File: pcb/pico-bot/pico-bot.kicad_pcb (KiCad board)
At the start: 2 copper layers, 58 parts, among them J1 Conn_01x02_Male, J2 Conn_01x06_Male, J3 Conn_01x06_Male, J4 Conn_01x06_Male, J5 Conn_01x06_Male, Q1 DMG2305UX, Q2 AOD417, SW1 SW_SPDT, SW2 SW_Push, SW3 SW_Push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

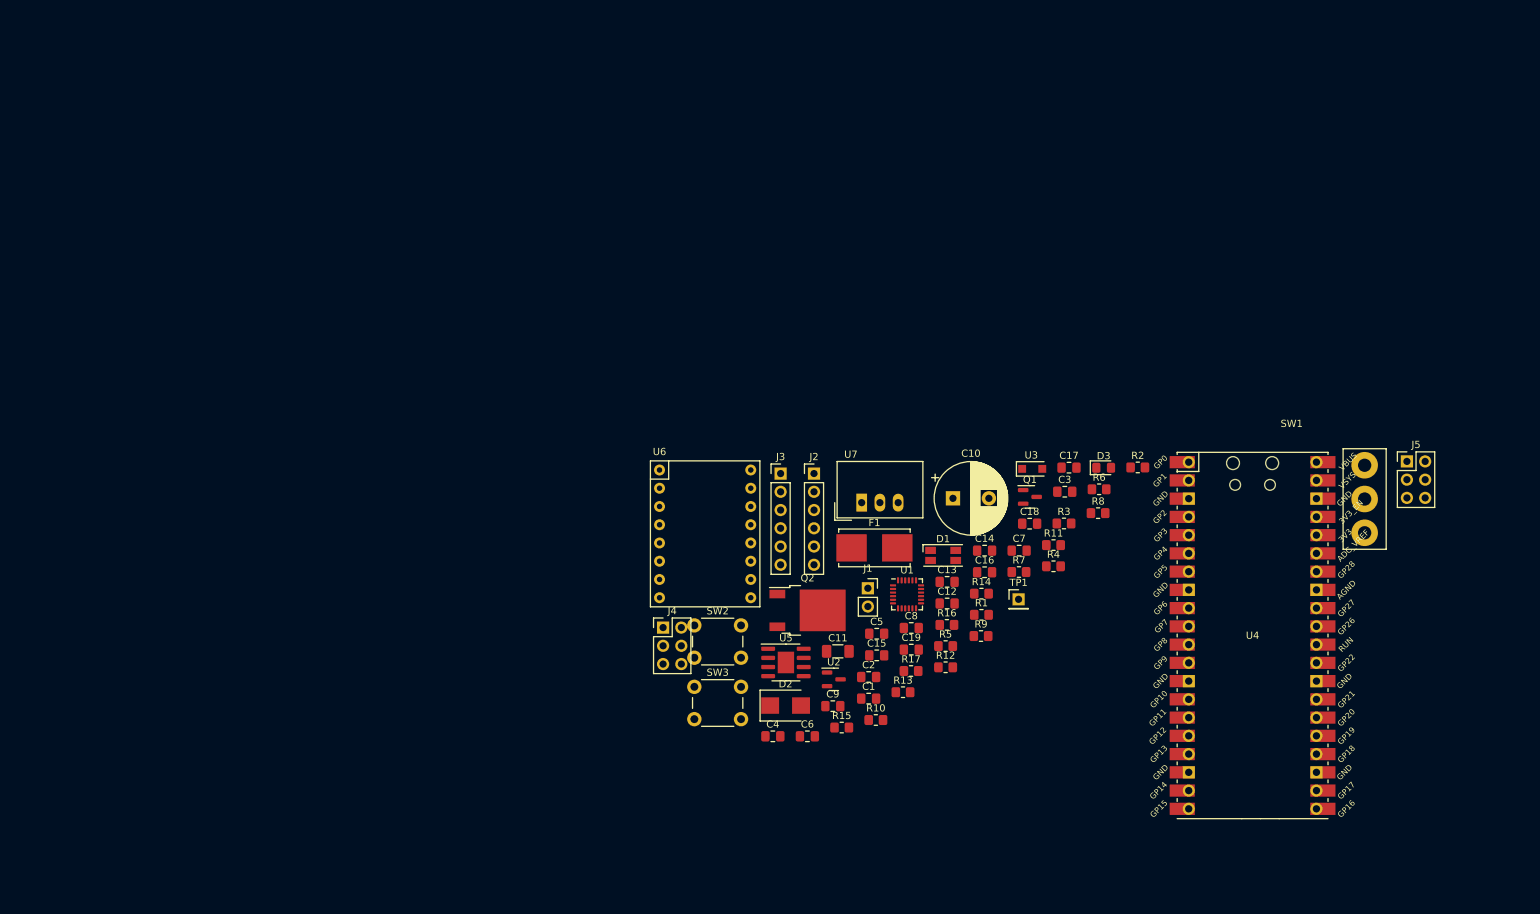
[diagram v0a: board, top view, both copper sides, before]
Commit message: Define mounting hole locations
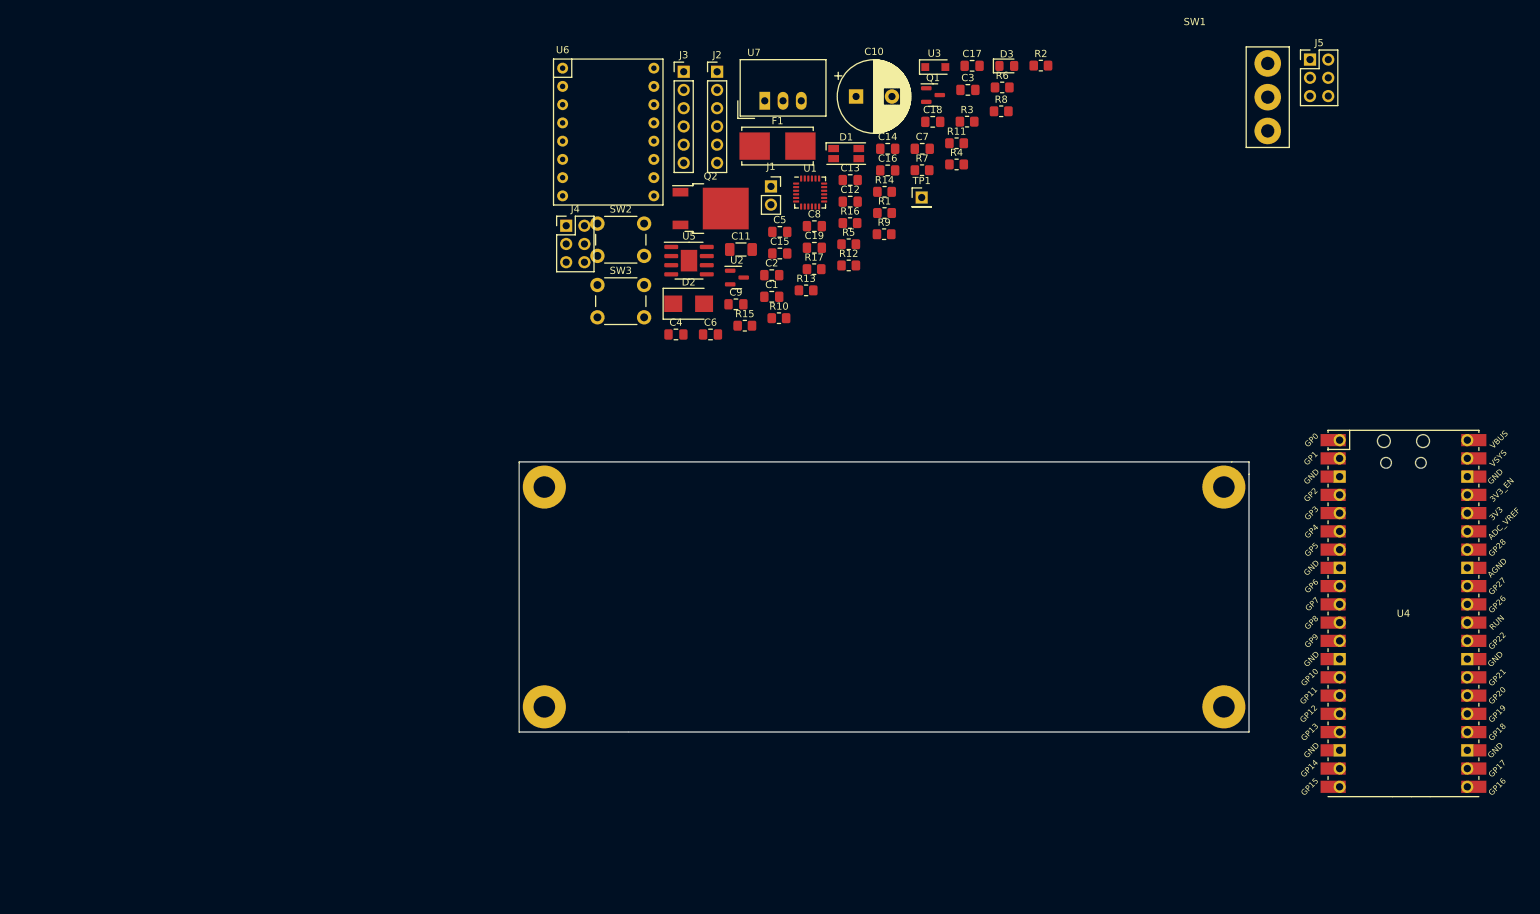
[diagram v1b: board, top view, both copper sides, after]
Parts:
- added REF**: MountingHole_3mm_Pad, MountingHole:MountingHole_3mm_Pad, F.Cu at (100.9, 109.1)
- added REF**: MountingHole_3mm_Pad, MountingHole:MountingHole_3mm_Pad, F.Cu at (100.9, 78.5)
- added REF**: MountingHole_3mm_Pad, MountingHole:MountingHole_3mm_Pad, F.Cu at (195.5, 78.5)
- added REF**: MountingHole_3mm_Pad, MountingHole:MountingHole_3mm_Pad, F.Cu at (195.5, 109.1)
- moved J5 57.5 mm to (207.5, 19.0)
- moved C1 57.5 mm to (132.6, 52.0)
- moved C11 57.5 mm to (128.3, 45.4)
- moved C13 57.5 mm to (143.5, 35.8)
- moved C15 57.5 mm to (133.7, 46.0)
- moved C3 57.5 mm to (159.9, 23.2)
- moved C4 57.5 mm to (119.2, 57.3)
- moved C5 57.5 mm to (133.7, 43.0)
- moved C6 57.5 mm to (124.0, 57.3)
- moved C8 57.5 mm to (138.5, 42.2)
- moved D2 57.5 mm to (121.0, 53.0)
- moved J1 57.5 mm to (132.4, 36.6)
- moved J2 57.5 mm to (125.0, 20.7)
- moved J3 57.5 mm to (120.3, 20.7)
- moved J4 57.5 mm to (103.9, 42.1)
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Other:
- board outline added: 101.6 x 37.6 mm

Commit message: Group circuits together on PCB
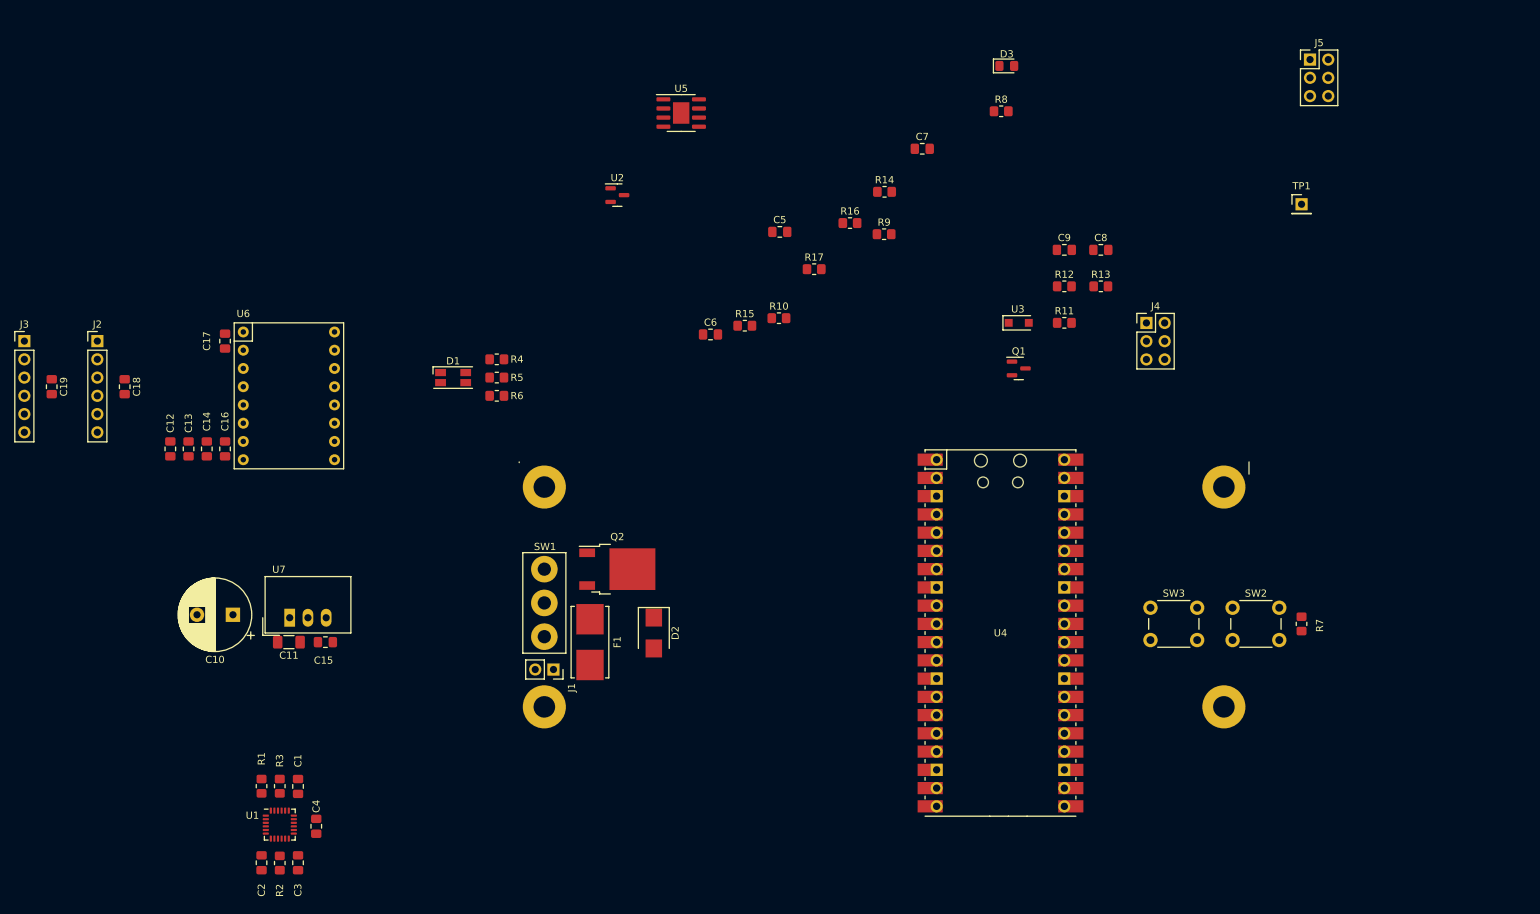
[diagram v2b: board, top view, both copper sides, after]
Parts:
- moved R2 153.5 mm to (64.1, 130.8), turned to 90 degrees
- moved C3 142.4 mm to (66.6, 130.8), turned to 90 degrees
- moved R3 133.1 mm to (64.1, 120.1), turned to 90 degrees
- moved SW1 122.9 mm to (100.9, 89.9)
- moved C18 118.4 mm to (42.5, 64.5), turned to -90 degrees
- moved R1 117.8 mm to (61.5, 120.1), turned to 90 degrees
- moved U1 114.9 mm to (64.1, 125.5)
- moved C10 112.8 mm to (57.5, 96.3), turned to 180 degrees
- moved C17 110.8 mm to (56.5, 58.2), turned to -90 degrees
- moved C2 108.3 mm to (61.5, 130.8), turned to 90 degrees
- moved C19 107.9 mm to (32.3, 64.5), turned to -90 degrees
- moved C14 103.6 mm to (53.9, 73.2), turned to 90 degrees
- moved SW2 103.3 mm to (196.7, 95.3)
- moved C12 100.7 mm to (48.8, 73.2), turned to 90 degrees
- moved C16 100.1 mm to (56.5, 73.2), turned to 90 degrees
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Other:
- board size 101.6 x 37.6 mm -> 101.6 x 1.7 mm

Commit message: Group undervoltage protection circuit components
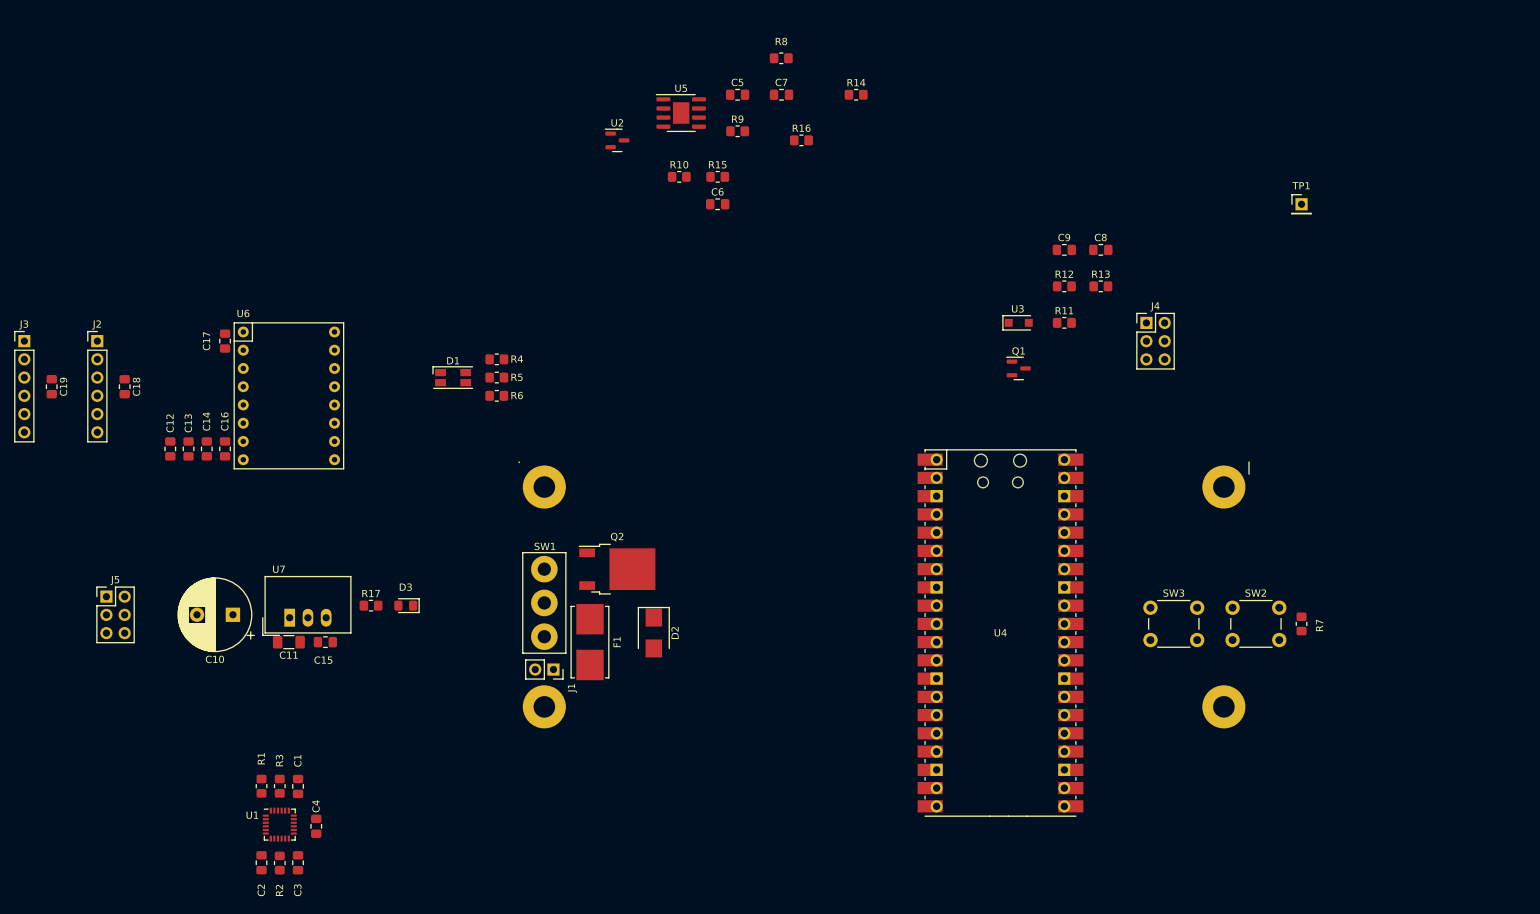
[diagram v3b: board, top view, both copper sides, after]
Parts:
- moved J5 183.5 mm to (39.9, 93.8)
- moved D3 112.5 mm to (81.6, 95.0), turned to 180 degrees
- moved R17 77.5 mm to (76.8, 95.0)
- moved R8 31.5 mm to (133.9, 18.8)
- moved R9 24.9 mm to (127.8, 29.0)
- moved R10 24.1 mm to (119.7, 35.3)
- moved R15 21.1 mm to (125.0, 35.3)
- moved C7 21.0 mm to (133.9, 23.9)
- moved C5 20.0 mm to (127.8, 23.9)
- moved C6 18.2 mm to (125.0, 39.1)
- moved R14 14.1 mm to (144.3, 23.9)
- moved R16 13.3 mm to (136.7, 30.2)
- moved U2 7.62 mm to (111.1, 30.2)
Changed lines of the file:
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@@
   )
   (footprint "Resistor_SMD:R_0805_2012Metric_Pad1.20x1.40mm_HandSolder" (layer "F.Cu")
-    (at 133.56 54.99)
+    (at 119.68 35.32)
     (descr "Resistor SMD 0805 (2012 Metric), square (rectangular) end terminal, IPC_7351 nominal with elongated pad for handsoldering. (Body size source: IPC-SM-782 page 72, https://www.pcb-3d.com/wordpress/wp-content/uploads/ipc-sm-782a_amendment_1_and_2.pdf), generated with kicad-footprint-generator")
     (tags "resistor handsolder")
@@
   )
   (footprint "Resistor_SMD:R_0805_2012Metric_Pad1.20x1.40mm_HandSolder" (layer "F.Cu")
-    (at 148.2 43.3)
+    (at 127.8025 28.97)
     (descr "Resistor SMD 0805 (2012 Metric), square (rectangular) end terminal, IPC_7351 nominal with elongated pad for handsoldering. (Body size source: IPC-SM-782 page 72, https://www.pcb-3d.com/wordpress/wp-content/uploads/ipc-sm-782a_amendment_1_and_2.pdf), generated with kicad-footprint-generator")
     (tags "resistor handsolder")
@@
   )
   (footprint "Capacitor_SMD:C_0805_2012Metric_Pad1.18x1.45mm_HandSolder" (layer "F.Cu")
-    (at 153.51 31.41)
+    (at 133.92 23.89)
     (descr "Capacitor SMD 0805 (2012 Metric), square (rectangular) end terminal, IPC_7351 nominal with elongated pad for handsoldering. (Body size source: IPC-SM-782 page 76, https://www.pcb-3d.com/wordpress/wp-content/uploads/ipc-sm-782a_amendment_1_and_2.pdf, https://docs.google.com/spreadsheets/d/1BsfQQcO9C6DZCsRaXUlFlo91Tg2WpOkGARC1WS5S8t0/edit?usp=sharing), generated with kicad-footprint-generator")
     (tags "capacitor handsolder")
@@
   )
   (footprint "Capacitor_SMD:C_0805_2012Metric_Pad1.18x1.45mm_HandSolder" (layer "F.Cu")
-    (at 124.03 57.26)
+    (at 125.03 39.13)
     (descr "Capacitor SMD 0805 (2012 Metric), square (rectangular) end terminal, IPC_7351 nominal with elongated pad for handsoldering. (Body size source: IPC-SM-782 page 76, https://www.pcb-3d.com/wordpress/wp-content/uploads/ipc-sm-782a_amendment_1_and_2.pdf, https://docs.google.com/spreadsheets/d/1BsfQQcO9C6DZCsRaXUlFlo91Tg2WpOkGARC1WS5S8t0/edit?usp=sharing), generated with kicad-footprint-generator")
     (tags "capacitor handsolder")
@@
   )
   (footprint "Package_TO_SOT_SMD:SOT-23" (layer "F.Cu")
-    (at 111.06 37.86)
+    (at 111.06 30.24)
     (descr "SOT, 3 Pin (https://www.jedec.org/system/files/docs/to-236h.pdf variant AB), generated with kicad-footprint-generator ipc_gullwing_generator.py")
     (tags "SOT TO_SOT_SMD")
@@
   )
   (footprint "LED_SMD:LED_0805_2012Metric_Pad1.15x1.40mm_HandSolder" (layer "F.Cu")
-    (at 165.275 19.875)
+    (at 81.605 95.01 180)
     (descr "LED SMD 0805 (2012 Metric), square (rectangular) end terminal, IPC_7351 nominal, (Body size source: https://docs.google.com/spreadsheets/d/1BsfQQcO9C6DZCsRaXUlFlo91Tg2WpOkGARC1WS5S8t0/edit?usp=sharing), generated with kicad-footprint-generator")
     (tags "LED handsolder")
@@
     (property "Sheetname" "")
     (attr smd)
-    (fp_text reference "D3" (at 0 -1.65) (layer "F.SilkS")
+    (fp_text reference "D3" (at 0 2.54) (layer "F.SilkS")
       (effects (font (size 1 1) (thickness 0.15)))
     )
@@
     (fp_line (start -1 -0.3) (end -1 0.6) (layer "F.Fab") (width 0.1))
     (fp_line (start -1 0.6) (end 1 0.6) (layer "F.Fab") (width 0.1))
-    (pad "1" smd roundrect (at -1.025 0) (size 1.15 1.4) (layers "F.Cu" "F.Paste" "F.Mask") (roundrect_rratio 0.217391)
+    (pad "1" smd roundrect (at -1.025 0 180) (size 1.15 1.4) (layers "F.Cu" "F.Paste" "F.Mask") (roundrect_rratio 0.217391)
       (net 1 "GND") (pinfunction "K") (pintype "passive"))
-    (pad "2" smd roundrect (at 1.025 0) (size 1.15 1.4) (layers "F.Cu" "F.Paste" "F.Mask") (roundrect_rratio 0.217391)
+    (pad "2" smd roundrect (at 1.025 0 180) (size 1.15 1.4) (layers "F.Cu" "F.Paste" "F.Mask") (roundrect_rratio 0.217391)
       (net 14 "Net-(D3-Pad2)") (pinfunction "A") (pintype "passive"))
     (model "${KICAD6_3DMODEL_DIR}/LED_SMD.3dshapes/LED_0805_2012Metric.wrl"
@@
   )
   (footprint "Capacitor_SMD:C_0805_2012Metric_Pad1.18x1.45mm_HandSolder" (layer "F.Cu")
-    (at 133.68 42.98)
+    (at 127.8025 23.89)
     (descr "Capacitor SMD 0805 (2012 Metric), square (rectangular) end terminal, IPC_7351 nominal with elongated pad for handsoldering. (Body size source: IPC-SM-782 page 76, https://www.pcb-3d.com/wordpress/wp-content/uploads/ipc-sm-782a_amendment_1_and_2.pdf, https://docs.google.com/spreadsheets/d/1BsfQQcO9C6DZCsRaXUlFlo91Tg2WpOkGARC1WS5S8t0/edit?usp=sharing), generated with kicad-footprint-generator")
     (tags "capacitor handsolder")
@@
   )
   (footprint "Resistor_SMD:R_0805_2012Metric_Pad1.20x1.40mm_HandSolder" (layer "F.Cu")
-    (at 138.46 48.17)
+    (at 76.77 95.01)
     (descr "Resistor SMD 0805 (2012 Metric), square (rectangular) end terminal, IPC_7351 nominal with elongated pad for handsoldering. (Body size source: IPC-SM-782 page 72, https://www.pcb-3d.com/wordpress/wp-content/uploads/ipc-sm-782a_amendment_1_and_2.pdf), generated with kicad-footprint-generator")
     (tags "resistor handsolder")
@@
   )
   (footprint "Connector_PinHeader_2.54mm:PinHeader_2x03_P2.54mm_Vertical" (layer "F.Cu")
-    (at 207.49 18.99)
+    (at 39.935 93.755)
     (descr "Through hole straight pin header, 2x03, 2.54mm pitch, double rows")
     (tags "Through hole pin header THT 2x03 2.54mm double row")
@@
   )
   (footprint "Resistor_SMD:R_0805_2012Metric_Pad1.20x1.40mm_HandSolder" (layer "F.Cu")
-    (at 143.45 41.75)
+    (at 136.6925 30.24)
     (descr "Resistor SMD 0805 (2012 Metric), square (rectangular) end terminal, IPC_7351 nominal with elongated pad for handsoldering. (Body size source: IPC-SM-782 page 72, https://www.pcb-3d.com/wordpress/wp-content/uploads/ipc-sm-782a_amendment_1_and_2.pdf), generated with kicad-footprint-generator")
     (tags "resistor handsolder")
@@
   )
   (footprint "Resistor_SMD:R_0805_2012Metric_Pad1.20x1.40mm_HandSolder" (layer "F.Cu")
-    (at 148.26 37.4)
+    (at 144.3125 23.89)
     (descr "Resistor SMD 0805 (2012 Metric), square (rectangular) end terminal, IPC_7351 nominal with elongated pad for handsoldering. (Body size source: IPC-SM-782 page 72, https://www.pcb-3d.com/wordpress/wp-content/uploads/ipc-sm-782a_amendment_1_and_2.pdf), generated with kicad-footprint-generator")
     (tags "resistor handsolder")
@@
   )
   (footprint "Resistor_SMD:R_0805_2012Metric_Pad1.20x1.40mm_HandSolder" (layer "F.Cu")
-    (at 128.81 56.04)
+    (at 125.03 35.32)
     (descr "Resistor SMD 0805 (2012 Metric), square (rectangular) end terminal, IPC_7351 nominal with elongated pad for handsoldering. (Body size source: IPC-SM-782 page 72, https://www.pcb-3d.com/wordpress/wp-content/uploads/ipc-sm-782a_amendment_1_and_2.pdf), generated with kicad-footprint-generator")
     (tags "resistor handsolder")
@@
   )
   (footprint "Resistor_SMD:R_0805_2012Metric_Pad1.20x1.40mm_HandSolder" (layer "F.Cu")
-    (at 164.5 26.19)
+    (at 133.8825 18.81)
     (descr "Resistor SMD 0805 (2012 Metric), square (rectangular) end terminal, IPC_7351 nominal with elongated pad for handsoldering. (Body size source: IPC-SM-782 page 72, https://www.pcb-3d.com/wordpress/wp-content/uploads/ipc-sm-782a_amendment_1_and_2.pdf), generated with kicad-footprint-generator")
     (tags "resistor handsolder")
@@
     (property "Sheetname" "")
     (attr smd)
-    (fp_text reference "R8" (at 0 -1.65) (layer "F.SilkS")
-      (effects (font (size 1 1) (thickness 0.15)))
-    )
+    (fp_text reference "R8" (at 0 -2.3) (layer "F.SilkS")
+      (effects (font (size 1 1) (thickness 0.15)))
+    )
